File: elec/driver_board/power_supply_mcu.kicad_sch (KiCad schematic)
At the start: 4 parts

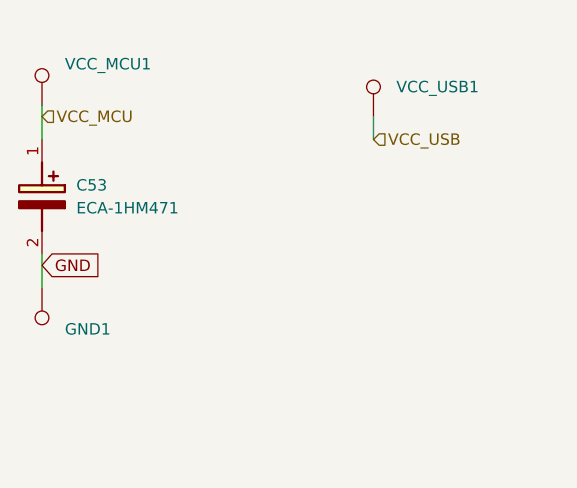
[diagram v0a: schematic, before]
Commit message: [elec] New design with BKA30D-R5
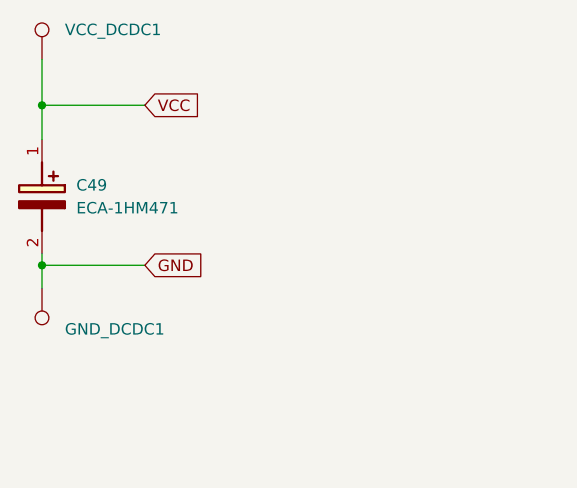
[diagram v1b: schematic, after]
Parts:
- removed VCC_USB1: M+, TestPoint:TestPoint_Keystone_5000-5004_Miniature, symbol Connector:TestPoint
- renumbered C53 to C49, GND1 to GND_DCDC1, VCC_MCU1 to VCC_DCDC1
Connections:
- net VCC_MCU renamed VCC
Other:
- title: (none) -> Power supply
- moved on the sheet: VCC_DCDC1
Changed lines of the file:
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@@
 	(generator_version "8.0")
 	(paper "A4")
-	(wire
-		(pts
-			(xy 133.35 68.58) (xy 133.35 71.12)
-		)
-		(stroke
-			(width 0)
-			(type default)
-		)
-	)
-	(wire
-		(pts
-			(xy 96.52 83.82) (xy 96.52 87.63)
+	(title_block
+		(title "Power supply")
+		(date "2024-11-23")
+		(rev "1")
+	)
+	(junction
+		(at 96.52 85.09)
+		(diameter 0)
+		(color 0 0 0 0)
+	)
+	(junction
+		(at 96.52 67.31)
+		(diameter 0)
+		(color 0 0 0 0)
+	)
+	(wire
+		(pts
+			(xy 96.52 85.09) (xy 96.52 87.63)
+		)
+		(stroke
+			(width 0)
+			(type default)
+		)
+	)
+	(wire
+		(pts
+			(xy 107.95 67.31) (xy 96.52 67.31)
 		)
 		(stroke
@@
 		(pts
 			(xy 96.52 67.31) (xy 96.52 71.12)
+		)
+		(stroke
+			(width 0)
+			(type default)
+		)
+	)
+	(wire
+		(pts
+			(xy 96.52 83.82) (xy 96.52 85.09)
+		)
+		(stroke
+			(width 0)
+			(type default)
+		)
+	)
+	(wire
+		(pts
+			(xy 96.52 62.23) (xy 96.52 67.31)
+		)
+		(stroke
+			(width 0)
+			(type default)
+		)
+	)
+	(wire
+		(pts
+			(xy 107.95 85.09) (xy 96.52 85.09)
 		)
 		(stroke
@@
 	(global_label "GND"
 		(shape input)
-		(at 96.52 85.09 0)
+		(at 107.95 85.09 0)
 		(fields_autoplaced yes)
 		(effects
@@
 		)
 		(property "Intersheetrefs" "${INTERSHEET_REFS}"
-			(at 103.3757 85.09 0)
-			(effects
-				(font
-					(size 1.27 1.27)
-				)
-				(justify left)
-				(hide yes)
-			)
-		)
-	)
-	(hierarchical_label "VCC_USB"
+			(at 114.8057 85.09 0)
+			(effects
+				(font
+					(size 1.27 1.27)
+				)
+				(justify left)
+				(hide yes)
+			)
+		)
+	)
+	(global_label "VCC"
 		(shape input)
-		(at 133.35 71.12 0)
+		(at 107.95 67.31 0)
 		(fields_autoplaced yes)
 		(effects
@@
 			(justify left)
 		)
-	)
-	(hierarchical_label "VCC_MCU"
-		(shape input)
-		(at 96.52 68.58 0)
+		(property "Intersheetrefs" "${INTERSHEET_REFS}"
+			(at 114.5638 67.31 0)
+			(effects
+				(font
+					(size 1.27 1.27)
+				)
+				(justify left)
+				(hide yes)
+			)
+		)
+	)
+	(netclass_flag ""
+		(length 2.54)
+		(shape round)
+		(at 96.52 67.31 90)
 		(fields_autoplaced yes)
 		(effects
@@
 				(size 1.27 1.27)
 			)
-			(justify left)
+			(justify left bottom)
+		)
+		(property "Netclass" "power"
+			(at 93.98 66.6115 90)
+			(effects
+				(font
+					(size 1.27 1.27)
+					(italic yes)
+				)
+				(justify left)
+			)
 		)
 	)
@@
 		(on_board yes)
 		(dnp no)
-		(property "Reference" "GND1"
+		(property "Reference" "GND_DCDC1"
 			(at 99.06 92.2021 0)
 			(effects
@@
 			(project "driver_board"
 				(path "/f74582a2-e122-4df8-8bf1-319684e69fbe/8c6a74a5-4238-4c38-a1b6-74fe6b2385f9"
-					(reference "GND1")
+					(reference "GND_DCDC1")
 					(unit 1)
 				)
@@
 		(dnp no)
 		(fields_autoplaced yes)
-		(property "Reference" "C53"
+		(property "Reference" "C49"
 			(at 100.33 76.1999 90)
 			(effects
@@
 			(project "driver_board"
 				(path "/f74582a2-e122-4df8-8bf1-319684e69fbe/8c6a74a5-4238-4c38-a1b6-74fe6b2385f9"
-					(reference "C53")
+					(reference "C49")
 					(unit 1)
 				)
@@
 	(symbol
 		(lib_id "Connector:TestPoint")
-		(at 133.35 68.58 0)
+		(at 96.52 62.23 0)
 		(unit 1)
 		(exclude_from_sim no)
@@
 		(dnp no)
 		(fields_autoplaced yes)
-		(property "Reference" "VCC_USB1"
-			(at 135.89 65.2779 0)
+		(property "Reference" "VCC_DCDC1"
+			(at 99.06 58.9279 0)
 			(effects
 				(font
@@
 		)
 		(property "Value" "M+"
-			(at 135.89 66.5479 0)
+			(at 99.06 60.1979 0)
 			(effects
 				(font
@@
 		)
 		(property "Footprint" "TestPoint:TestPoint_Keystone_5000-5004_Miniature"
-			(at 138.43 68.58 0)
+			(at 101.6 62.23 0)
 			(effects
 				(font
@@
 		)
 		(property "Datasheet" "~"
-			(at 138.43 68.58 0)
+			(at 101.6 62.23 0)
 			(effects
 				(font
@@
 		)
 		(property "Description" "test point"
-			(at 133.35 68.58 0)
+			(at 96.52 62.23 0)
 			(effects
 				(font
@@
 			(project "driver_board"
 				(path "/f74582a2-e122-4df8-8bf1-319684e69fbe/8c6a74a5-4238-4c38-a1b6-74fe6b2385f9"
-					(reference "VCC_USB1")
+					(reference "VCC_DCDC1")
 					(unit 1)
 				)
-			)
-		)
-	)
-	(symbol
-		(lib_id "Connector:TestPoint")
-		(at 96.52 67.31 0)
-		(unit 1)
-		(exclude_from_sim no)
-		(in_bom yes)
-		(on_board yes)
-		(dnp no)
-		(fields_autoplaced yes)
-		(property "Reference" "VCC_MCU1"
-			(at 99.06 62.7379 0)
-			(effects
-				(font
-					(size 1.27 1.27)
-				)
-				(justify left)
-			)
-		)
-		(property "Value" "M+"
-			(at 99.06 65.2779 0)
-			(effects
-				(font
-					(size 1.27 1.27)
-				)
-				(justify left)
-				(hide yes)
-			)
-		)
-		(property "Footprint" "TestPoint:TestPoint_Keystone_5000-5004_Miniature"
-			(at 101.6 67.31 0)
-			(effects
-				(font
-					(size 1.27 1.27)
-				)
-				(hide yes)
-			)
-		)
-		(property "Datasheet" "~"
-			(at 101.6 67.31 0)
-			(effects
-				(font
-					(size 1.27 1.27)
-				)
-				(hide yes)
-			)
-		)
-		(property "Description" "test point"
-			(at 96.52 67.31 0)
-			(effects
-				(font
-					(size 1.27 1.27)
-				)
-				(hide yes)
-			)
-		)
-		(pin "1"
-		)
-		(instances
-			(project "driver_board"
-				(path "/f74582a2-e122-4df8-8bf1-319684e69fbe/8c6a74a5-4238-4c38-a1b6-74fe6b2385f9"
-					(reference "VCC_MCU1")
-					(unit 1)
-				)

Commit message: [elec] First version of the routing of driver board
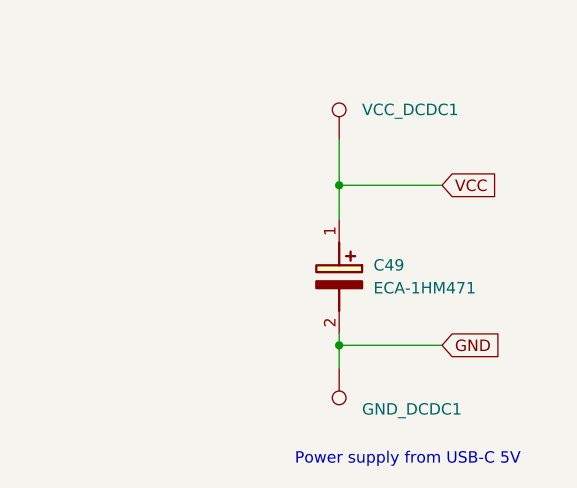
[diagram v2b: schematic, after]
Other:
- note added: "Power supply from USB-C 5V"
- moved on the sheet: C49, GND_DCDC1, VCC_DCDC1
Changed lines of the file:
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@@
 	)
 	(junction
-		(at 96.52 85.09)
+		(at 129.54 93.98)
 		(diameter 0)
 		(color 0 0 0 0)
 	)
 	(junction
-		(at 96.52 67.31)
+		(at 129.54 76.2)
 		(diameter 0)
 		(color 0 0 0 0)
@@
 	(wire
 		(pts
-			(xy 96.52 85.09) (xy 96.52 87.63)
-		)
-		(stroke
-			(width 0)
-			(type default)
-		)
-	)
-	(wire
-		(pts
-			(xy 107.95 67.31) (xy 96.52 67.31)
-		)
-		(stroke
-			(width 0)
-			(type default)
-		)
-	)
-	(wire
-		(pts
-			(xy 96.52 67.31) (xy 96.52 71.12)
-		)
-		(stroke
-			(width 0)
-			(type default)
-		)
-	)
-	(wire
-		(pts
-			(xy 96.52 83.82) (xy 96.52 85.09)
-		)
-		(stroke
-			(width 0)
-			(type default)
-		)
-	)
-	(wire
-		(pts
-			(xy 96.52 62.23) (xy 96.52 67.31)
-		)
-		(stroke
-			(width 0)
-			(type default)
-		)
-	)
-	(wire
-		(pts
-			(xy 107.95 85.09) (xy 96.52 85.09)
-		)
-		(stroke
-			(width 0)
-			(type default)
-		)
-	)
-	(global_label "GND"
-		(shape input)
-		(at 107.95 85.09 0)
-		(fields_autoplaced yes)
+			(xy 129.54 93.98) (xy 129.54 96.52)
+		)
+		(stroke
+			(width 0)
+			(type default)
+		)
+	)
+	(wire
+		(pts
+			(xy 140.97 76.2) (xy 129.54 76.2)
+		)
+		(stroke
+			(width 0)
+			(type default)
+		)
+	)
+	(wire
+		(pts
+			(xy 129.54 76.2) (xy 129.54 80.01)
+		)
+		(stroke
+			(width 0)
+			(type default)
+		)
+	)
+	(wire
+		(pts
+			(xy 129.54 92.71) (xy 129.54 93.98)
+		)
+		(stroke
+			(width 0)
+			(type default)
+		)
+	)
+	(wire
+		(pts
+			(xy 129.54 71.12) (xy 129.54 76.2)
+		)
+		(stroke
+			(width 0)
+			(type default)
+		)
+	)
+	(wire
+		(pts
+			(xy 140.97 93.98) (xy 129.54 93.98)
+		)
+		(stroke
+			(width 0)
+			(type default)
+		)
+	)
+	(text "Power supply from USB-C 5V"
+		(exclude_from_sim no)
+		(at 137.16 106.68 0)
 		(effects
 			(font
 				(size 1.27 1.27)
 			)
-			(justify left)
-		)
-		(property "Intersheetrefs" "${INTERSHEET_REFS}"
-			(at 114.8057 85.09 0)
-			(effects
-				(font
-					(size 1.27 1.27)
-				)
-				(justify left)
-				(hide yes)
-			)
-		)
-	)
-	(global_label "VCC"
+		)
+	)
+	(global_label "GND"
 		(shape input)
-		(at 107.95 67.31 0)
+		(at 140.97 93.98 0)
 		(fields_autoplaced yes)
 		(effects
@@
 		)
 		(property "Intersheetrefs" "${INTERSHEET_REFS}"
-			(at 114.5638 67.31 0)
+			(at 147.8257 93.98 0)
+			(effects
+				(font
+					(size 1.27 1.27)
+				)
+				(justify left)
+				(hide yes)
+			)
+		)
+	)
+	(global_label "VCC"
+		(shape input)
+		(at 140.97 76.2 0)
+		(fields_autoplaced yes)
+		(effects
+			(font
+				(size 1.27 1.27)
+			)
+			(justify left)
+		)
+		(property "Intersheetrefs" "${INTERSHEET_REFS}"
+			(at 147.5838 76.2 0)
 			(effects
 				(font
@@
 		(length 2.54)
 		(shape round)
-		(at 96.52 67.31 90)
+		(at 129.54 76.2 90)
 		(fields_autoplaced yes)
 		(effects
@@
 		)
 		(property "Netclass" "power"
-			(at 93.98 66.6115 90)
+			(at 127 75.5015 90)
 			(effects
 				(font
@@
 	(symbol
 		(lib_id "Connector:TestPoint")
-		(at 96.52 87.63 0)
+		(at 129.54 96.52 0)
 		(mirror x)
 		(unit 1)
@@
 		(dnp no)
 		(property "Reference" "GND_DCDC1"
-			(at 99.06 92.2021 0)
+			(at 132.08 101.0921 0)
 			(effects
 				(font
@@
 		)
 		(property "Value" "M-"
-			(at 99.06 89.6621 0)
+			(at 132.08 98.5521 0)
 			(effects
 				(font
@@
 		)
 		(property "Footprint" "TestPoint:TestPoint_Keystone_5000-5004_Miniature"
-			(at 101.6 87.63 0)
+			(at 134.62 96.52 0)
 			(effects
 				(font
@@
 		)
 		(property "Datasheet" "~"
-			(at 101.6 87.63 0)
+			(at 134.62 96.52 0)
 			(effects
 				(font
@@
 		)
 		(property "Description" "test point"
-			(at 96.52 87.63 0)
+			(at 129.54 96.52 0)
 			(effects
 				(font
@@
 	(symbol
 		(lib_id "Samacsys:ECA-1HM471")
-		(at 96.52 71.12 270)
+		(at 129.54 80.01 270)
 		(unit 1)
 		(exclude_from_sim no)
@@
 		(fields_autoplaced yes)
 		(property "Reference" "C49"
-			(at 100.33 76.1999 90)
+			(at 133.35 85.0899 90)
 			(effects
 				(font
@@
 		)
 		(property "Value" "ECA-1HM471"
-			(at 100.33 78.7399 90)
+			(at 133.35 87.6299 90)
 			(effects
 				(font
@@
 		)
 		(property "Footprint" "Samacsys:CAPPRD500W65D1000H2200"
-			(at 0.33 80.01 0)
+			(at 33.35 88.9 0)
 			(effects
 				(font
@@
 		)
 		(property "Datasheet" "http://industrial.panasonic.com/cdbs/www-data/pdf/RDF0000/ABA0000C1218.pdf"
-			(at -99.67 80.01 0)
+			(at -66.65 88.9 0)
 			(effects
 				(font
@@
 		)
 		(property "Description" "PANASONIC - ECA-1HM471 - Electrolytic Capacitor, 470 F, 50 V, M Series, +/- 20%, Radial Leaded, 10 mm"
-			(at 96.52 71.12 0)
+			(at 129.54 80.01 0)
 			(effects
 				(font
@@
 		)
 		(property "Height" "22"
-			(at -299.67 80.01 0)
+			(at -266.65 88.9 0)
 			(effects
 				(font
@@
 		)
 		(property "Manufacturer_Name" "Panasonic"
-			(at -399.67 80.01 0)
+			(at -366.65 88.9 0)
 			(effects
 				(font
@@
 		)
 		(property "Manufacturer_Part_Number" "ECA-1HM471"
-			(at -499.67 80.01 0)
+			(at -466.65 88.9 0)
 			(effects
 				(font
@@
 		)
 		(property "Arrow Part Number" "ECA-1HM471"
-			(at -599.67 80.01 0)
+			(at -566.65 88.9 0)
 			(effects
 				(font
@@
 		)
 		(property "Arrow Price/Stock" "https://www.arrow.com/en/products/eca-1hm471/panasonic"
-			(at -699.67 80.01 0)
+			(at -666.65 88.9 0)
 			(effects
 				(font
@@
 	(symbol
 		(lib_id "Connector:TestPoint")
-		(at 96.52 62.23 0)
+		(at 129.54 71.12 0)
 		(unit 1)
 		(exclude_from_sim no)
@@
 		(fields_autoplaced yes)
 		(property "Reference" "VCC_DCDC1"
-			(at 99.06 58.9279 0)
+			(at 132.08 67.8179 0)
 			(effects
 				(font
@@
 		)
 		(property "Value" "M+"
-			(at 99.06 60.1979 0)
+			(at 132.08 69.0879 0)
 			(effects
 				(font
@@
 		)
 		(property "Footprint" "TestPoint:TestPoint_Keystone_5000-5004_Miniature"
-			(at 101.6 62.23 0)
+			(at 134.62 71.12 0)
 			(effects
 				(font
@@
 		)
 		(property "Datasheet" "~"
-			(at 101.6 62.23 0)
+			(at 134.62 71.12 0)
 			(effects
 				(font
@@
 		)
 		(property "Description" "test point"
-			(at 96.52 62.23 0)
-			(effects
-				(font
+			(at 129.54 71.12 0)
+			(effects
+				(font

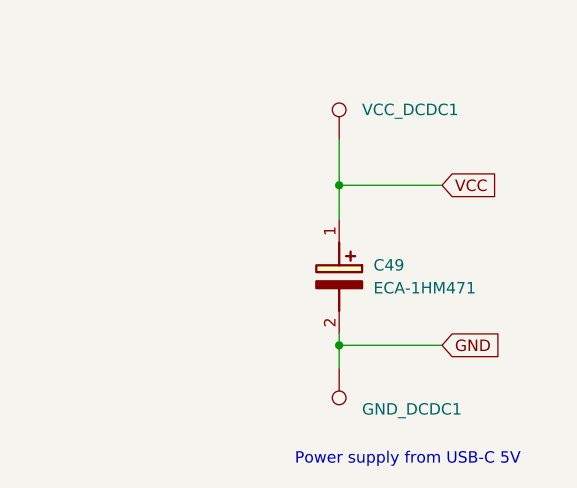
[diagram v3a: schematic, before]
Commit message: Update schematic with VID6606
Use the 'official' driver of VID28-05 motors.
Put back the 74HCT595 bit shift register to link all
motor drivers.
Work in progress.
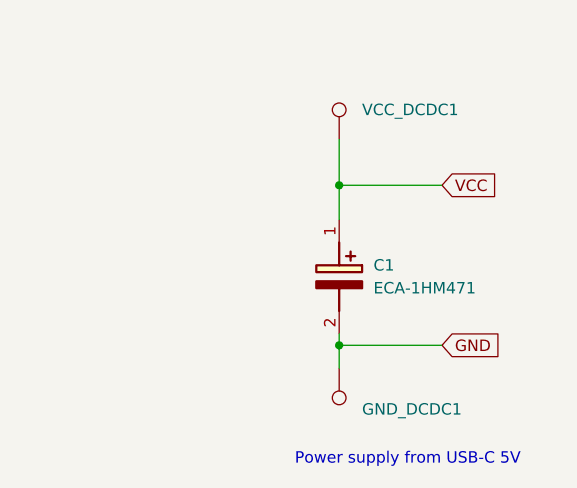
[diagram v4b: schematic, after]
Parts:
- renumbered C49 to C1
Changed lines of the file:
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@@
 		(dnp no)
 		(fields_autoplaced yes)
-		(property "Reference" "C49"
+		(property "Reference" "C1"
 			(at 133.35 85.0899 90)
 			(effects
@@
 			(project "driver_board"
 				(path "/f74582a2-e122-4df8-8bf1-319684e69fbe/8c6a74a5-4238-4c38-a1b6-74fe6b2385f9"
-					(reference "C49")
+					(reference "C1")
 					(unit 1)
 				)

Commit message: New schematic + route
The new design schematic is done.
Route is ongoing
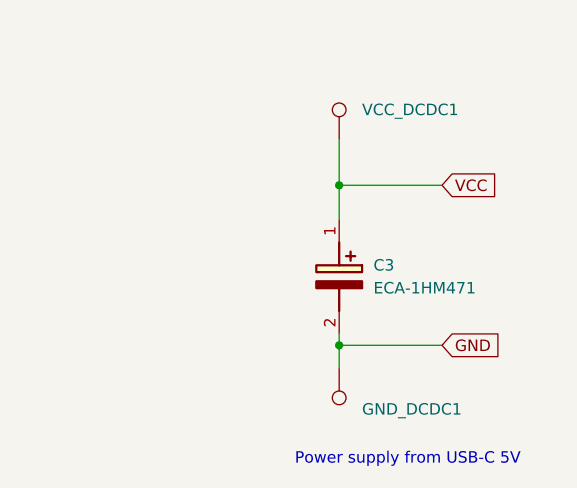
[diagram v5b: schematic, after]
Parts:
- renumbered C1 to C3
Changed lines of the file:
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@@
 		(dnp no)
 		(fields_autoplaced yes)
-		(property "Reference" "C1"
+		(property "Reference" "C3"
 			(at 133.35 85.0899 90)
 			(effects
@@
 			(project "driver_board"
 				(path "/f74582a2-e122-4df8-8bf1-319684e69fbe/8c6a74a5-4238-4c38-a1b6-74fe6b2385f9"
-					(reference "C1")
+					(reference "C3")
 					(unit 1)
 				)

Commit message: PCB done, ready to be ordered
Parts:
- GND_DCDC1: value M- -> GND
- VCC_DCDC1: value M+ -> VCC 5V
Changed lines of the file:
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@@
 	(title_block
 		(title "Power supply")
-		(date "2024-11-23")
-		(rev "1")
+		(date "2025-01-26")
+		(rev "2")
 	)
 	(junction
@@
 			)
 		)
-		(property "Value" "M-"
+		(property "Value" "GND"
 			(at 132.08 98.5521 0)
 			(effects
@@
 			)
 		)
-		(property "Value" "M+"
+		(property "Value" "VCC 5V"
 			(at 132.08 69.0879 0)
 			(effects

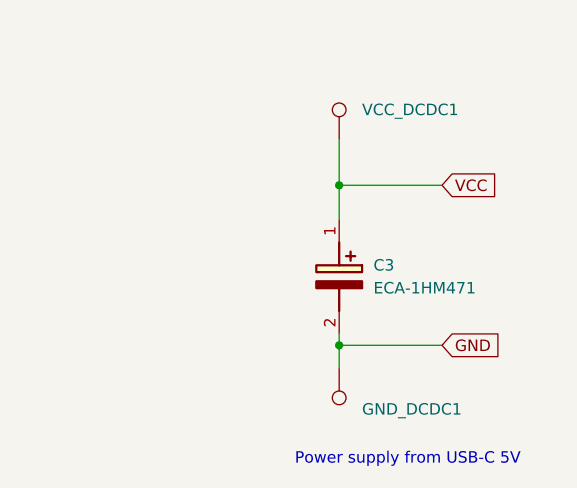
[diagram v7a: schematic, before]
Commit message: Various updates
Reposition rotary encoder
reposition RTC
add GND pads
update footprint of the big capa
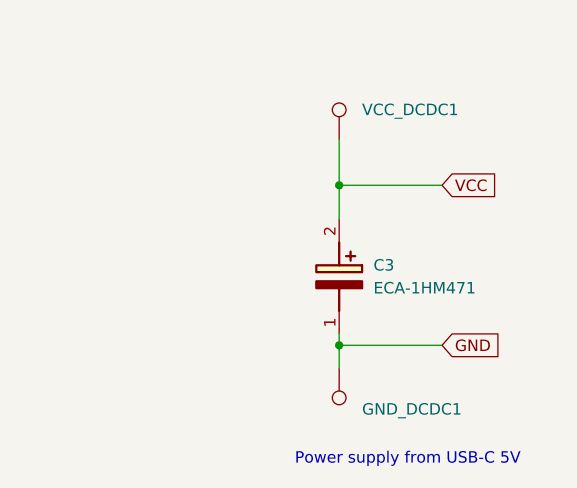
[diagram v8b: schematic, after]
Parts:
- GND_DCDC1: footprint TestPoint:TestPoint_Keystone_5000-5004_Miniature -> TestPoint:TestPoint_THTPad_2.0x2.0mm_Drill1.0mm
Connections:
- net GND: now also C3.1 (-); no longer C3.2 (-)
- net VCC: now also C3.2 (+); no longer C3.1 (+)
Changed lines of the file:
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@@
 			)
 		)
-		(property "Footprint" "TestPoint:TestPoint_Keystone_5000-5004_Miniature"
+		(property "Footprint" "TestPoint:TestPoint_THTPad_2.0x2.0mm_Drill1.0mm"
 			(at 134.62 96.52 0)
 			(effects
